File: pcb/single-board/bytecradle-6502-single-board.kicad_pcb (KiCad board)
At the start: 2 copper layers, 224.9 x 116.2 mm, 88 parts, among them J1 USB_B, J2 EXPBUS1, J3 EXPBUS2, J4 VIA, J5 UART1, J6 UART2, J7 Serial, J8 Serial, SW1 SW_SPDT, SW2 RESET, SW3 NMI, U1 74HC14, U10 74HC273, U11 74HC273, U12 74HC245, U13 74HC245, U14 74HC10, U15 SST39SF040, U16 AS6C4008, U17 CY62256, U18 74HC688, U19 W65C22NxP, U2 W65C02, U20 74HC688, U21 W65C51NxP, U22 74HC688, U23 W65C51NxP, U3 74HC688, U4 74HC08, U5 74HC688, U6 74HC688, U7 74HC04, U8 74HC10, U9 74HC00, X1 32MHz, Y1 1.8432 MHz, Y2 1.8432 MHz

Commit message: Further revising
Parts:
- added G***: LOGO, components:bytecradle-logo, F.Cu at (256.4, 48.5)
- X1: value 32MHz -> 14 MHz
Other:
- board text added: "jlcjlcjlcjlc"

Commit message: Updating design for V2
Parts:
- U1: value 74HC14 -> 74AC14
- U14, U8: value 74HC10 -> 74AC10
- U16: value AS6C4008 -> AS6C4008-55
- U17: value CY62256 -> 62256-55
- U18, U20, U22, U3, U5, U6: value 74HC688 -> CD74HC688
- U4: value 74HC08 -> 74AC08
- U7: value 74HC04 -> 74AC04
- U9: value 74HC00 -> 74AC00
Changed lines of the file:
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@@
 			)
 		)
-		(property "Value" "74HC688"
+		(property "Value" "CD74HC688"
 			(at 3.81 25.19 -90)
 			(layer "F.SilkS")
@@
 			)
 		)
-		(property "Value" "74HC688"
+		(property "Value" "CD74HC688"
 			(at 3.81 25.19 0)
 			(layer "F.SilkS")
@@
 		(property "Value" "100nF"
 			(at 2.5 2.54 90)
-			(layer "F.SilkS")
+			(layer "Dwgs.User")
 			(effects
 				(font
@@
 			)
 		)
-		(property "Value" "CY62256"
+		(property "Value" "62256-55"
 			(at 7.62 35.35 -90)
 			(layer "F.SilkS")
@@
 			)
 		)
-		(property "Value" "74HC688"
+		(property "Value" "CD74HC688"
 			(at 3.81 25.19 90)
-			(layer "F.Fab")
+			(layer "F.SilkS")
 			(effects
 				(font
@@
 			)
 		)
-		(property "Value" "74HC688"
+		(property "Value" "CD74HC688"
 			(at 3.81 25.19 -90)
 			(layer "F.SilkS")
@@
 			)
 		)
-		(property "Value" "74HC04"
+		(property "Value" "74AC04"
 			(at 3.81 17.57 -90)
 			(layer "F.SilkS")
@@
 			)
 		)
-		(property "Value" "AS6C4008"
+		(property "Value" "AS6C4008-55"
 			(at 7.62 40.43 90)
 			(layer "F.SilkS")
@@
 			)
 		)
-		(property "Value" "74HC10"
+		(property "Value" "74AC10"
 			(at 3.81 17.57 90)
 			(layer "F.SilkS")
@@
 			)
 		)
-		(property "Value" "74HC08"
+		(property "Value" "74AC08"
 			(at 3.81 17.57 -90)
 			(layer "F.SilkS")
@@
 			)
 		)
-		(property "Value" "74HC688"
+		(property "Value" "CD74HC688"
 			(at 3.81 25.19 0)
 			(layer "F.SilkS")
@@
 			)
 		)
-		(property "Value" "74HC10"
+		(property "Value" "74AC10"
 			(at 3.81 17.57 -90)
 			(layer "F.SilkS")
@@
 			)
 		)
-		(property "Value" "74HC14"
+		(property "Value" "74AC14"
 			(at 3.81 17.57 -90)
 			(layer "F.SilkS")
@@
 			)
 		)
-		(property "Value" "74HC00"
+		(property "Value" "74AC00"
 			(at 3.81 17.57 -90)
 			(layer "F.SilkS")
@@
 			)
 		)
-		(property "Value" "74HC688"
+		(property "Value" "CD74HC688"
 			(at 3.81 25.19 90)
 			(layer "F.SilkS")

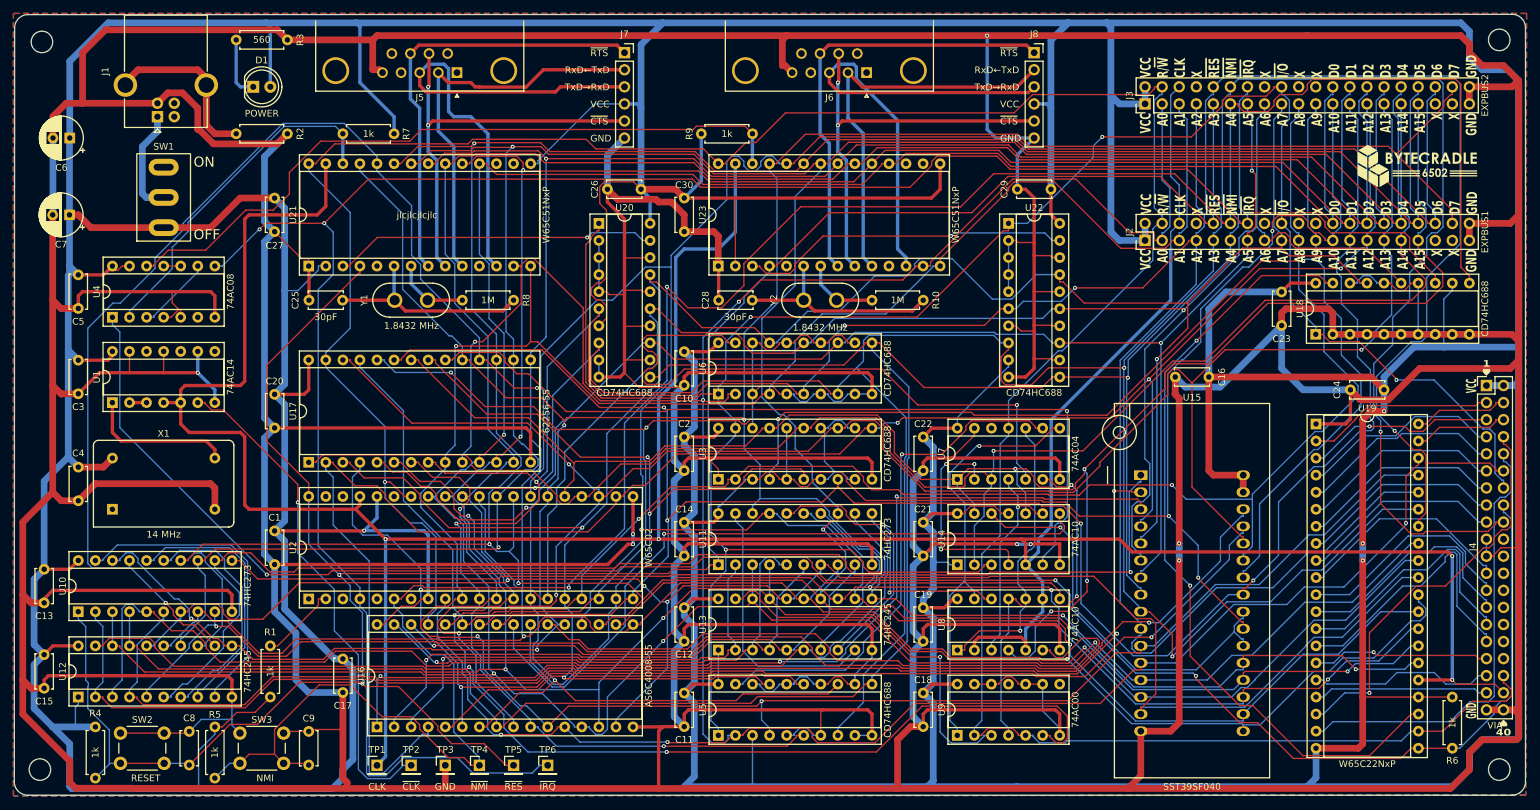
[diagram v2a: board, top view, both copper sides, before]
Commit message: Revising single board layout
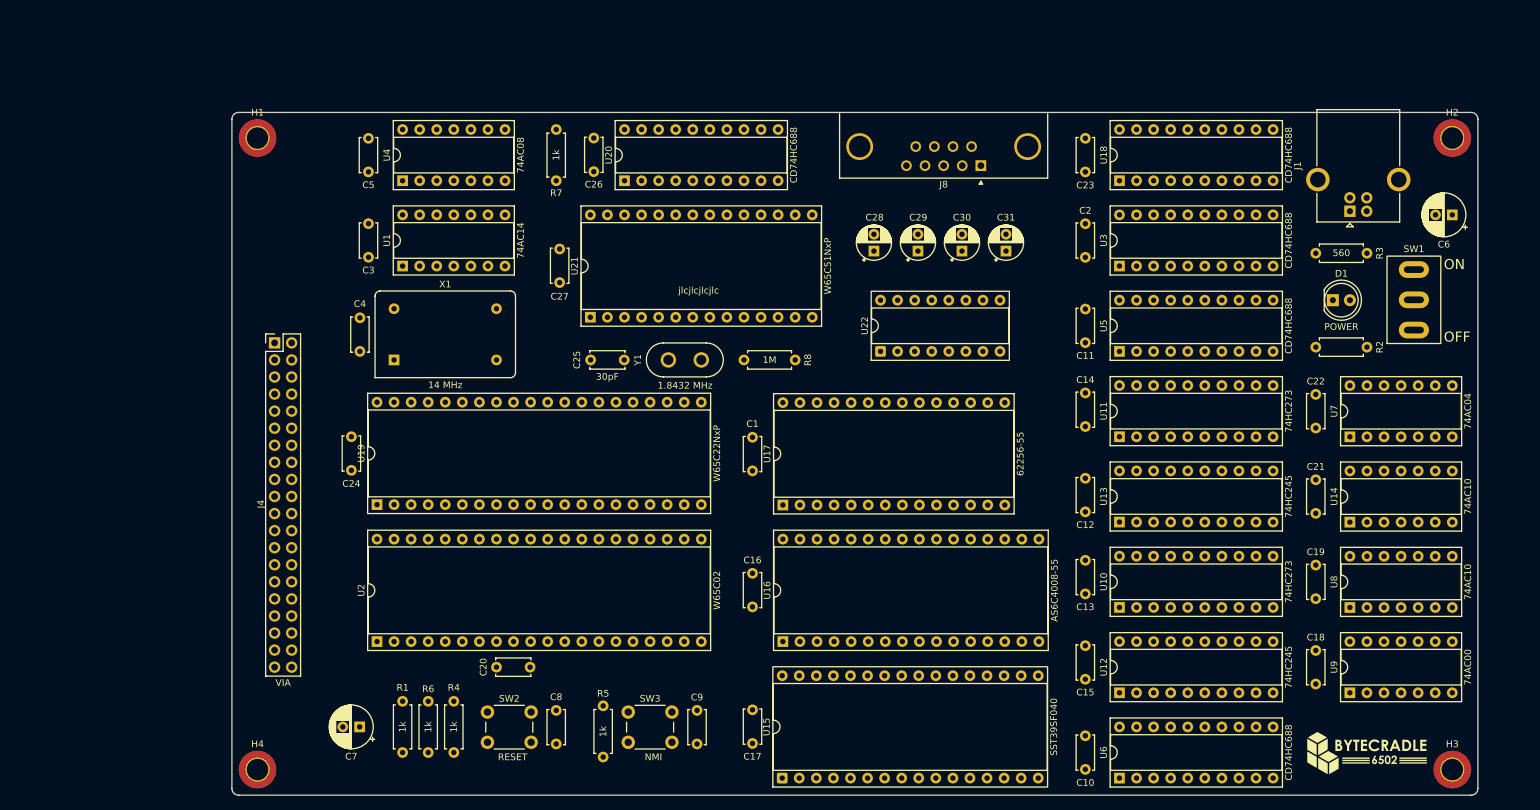
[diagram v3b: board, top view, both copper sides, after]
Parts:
- removed J2: EXPBUS1, Connector_PinHeader_2.54mm:PinHeader_2x20_P2.54mm_Vertical
- removed J3: EXPBUS2, Connector_PinHeader_2.54mm:PinHeader_2x20_P2.54mm_Vertical
- removed J5: UART1, Connector_Dsub:DSUB-9_Male_Horizontal_P2.77x2.84mm_EdgePinOffset4.94mm_Housed_MountingHolesOffset7.48mm
- removed J6: UART2, Connector_Dsub:DSUB-9_Male_Horizontal_P2.77x2.84mm_EdgePinOffset4.94mm_Housed_MountingHolesOffset7.48mm
- removed J7: Serial, Connector_PinSocket_2.54mm:PinSocket_1x06_P2.54mm_Vertical
- removed R10: 1M, Resistor_THT:R_Axial_DIN0207_L6.3mm_D2.5mm_P7.62mm_Horizontal
- removed R9: 1k, Resistor_THT:R_Axial_DIN0207_L6.3mm_D2.5mm_P7.62mm_Horizontal
- removed TP1: CLK, Connector_PinHeader_2.54mm:PinHeader_1x01_P2.54mm_Vertical
- removed TP2: ~{CLK}, Connector_PinHeader_2.54mm:PinHeader_1x01_P2.54mm_Vertical
- removed TP3: GND, Connector_PinHeader_2.54mm:PinHeader_1x01_P2.54mm_Vertical
- removed TP4: ~{NMI}, Connector_PinHeader_2.54mm:PinHeader_1x01_P2.54mm_Vertical
- removed TP5: ~{RES}, Connector_PinHeader_2.54mm:PinHeader_1x01_P2.54mm_Vertical
- removed TP6: ~{IRQ}, Connector_PinHeader_2.54mm:PinHeader_1x01_P2.54mm_Vertical
- removed U23: W65C51NxP, Package_DIP:DIP-28_W15.24mm_Socket
- removed Y2: 1.8432 MHz, Crystal:Crystal_HC50_Vertical
- added C31: 10uF, Capacitor_THT:CP_Radial_D5.0mm_P2.50mm, F.Cu at (195.2, 61.3)
- C28: value 30pF -> 10uF; footprint Capacitor_THT:C_Disc_D5.0mm_W2.5mm_P5.00mm -> Capacitor_THT:CP_Radial_D5.0mm_P2.50mm
- C29, C30: value 100nF -> 10uF; footprint Capacitor_THT:C_Disc_D5.0mm_W2.5mm_P5.00mm -> Capacitor_THT:CP_Radial_D5.0mm_P2.50mm
- C6: value 10uF -> 100uF
- H1, H2, H3, H4: footprint MountingHole:MountingHole_3.2mm_M3 -> MountingHole:MountingHole_3.2mm_M3_DIN965_Pad_TopOnly
- J8: value Serial -> UART1; footprint Connector_PinSocket_2.54mm:PinSocket_1x06_P2.54mm_Vertical -> Connector_Dsub:DSUB-9_Pins_Horizontal_P2.77x2.84mm_EdgePinOffset4.94mm_Housed_MountingHolesOffset4.94mm
- U15: footprint Socket:DIP_Socket-32_W11.9_W12.7_W15.24_W17.78_W18.5_3M_232-1285-00-0602J -> Package_DIP:DIP-32_W15.24mm_Socket
- U22: value CD74HC688 -> MAX232; footprint Package_DIP:DIP-20_W7.62mm_Socket -> Package_DIP:DIP-16_W7.62mm_Socket
- moved H3 210.2 mm to (261.6, 138.4)
- moved C6 206.1 mm to (261.6, 55.9)
- moved SW1 186.7 mm to (255.9, 68.5)
- moved H4 184.8 mm to (83.8, 138.4)
- moved J4 180.5 mm to (86.4, 74.9)
- moved J1 178.0 mm to (246.4, 55.3)
- moved D1 163.8 mm to (243.8, 68.6)
- moved R2 163.8 mm to (248.9, 75.6)
- moved R3 163.8 mm to (248.9, 61.6)
- moved C13 154.9 mm to (207.0, 107.3)
- moved C15 154.9 mm to (207.0, 120.0)
- moved U10 154.9 mm to (212.1, 114.3)
- moved U12 154.9 mm to (212.1, 127.0)
- moved C24 153.8 mm to (97.8, 88.9), turned to -90 degrees
- moved R6 152.6 mm to (109.2, 135.9), turned to 90 degrees
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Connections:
- C28 pad 1: GND -> Net-(U22-C1+)
- C28 pad 2: Net-(U23-XTAL1) -> Net-(U22-C1-)
- C29 pad 1: VCC -> Net-(U22-C2+)
- C29 pad 2: GND -> Net-(U22-C2-)
- C30 pad 1: VCC -> Net-(U22-VS+)
- C30 pad 2: GND -> VCC
- J8 pad 1: ~{RTS2} -> unconnected-(J8-Pad1)
- J8 pad 2: TxD2 -> Net-(U22-T1OUT)
- J8 pad 3: RxD2 -> Net-(U22-R1IN)
- J8 pad 4: VCC -> unconnected-(J8-Pad4)
- J8 pad 5: ~{CTS2} -> GND
- J8 pad 6: GND -> unconnected-(J8-Pad6)
- U21 pad 8: ~{RTS1} -> GND
- U21 pad 9: ~{CTS1} -> GND
- U22 pad 1: ~{I/O} -> Net-(U22-C1+)
- U22 pad 10: GND -> unconnected-(U22-T2IN-Pad10)
- U22 pad 11: A4 -> TxD1
- U22 pad 12: GND -> RxD1
- U22 pad 13: A5 -> Net-(U22-R1IN)
- U22 pad 14: GND -> Net-(U22-T1OUT)
- U22 pad 15: A6 -> GND
- U22 pad 16: GND -> VCC
- U22 pad 2: GND -> Net-(U22-VS+)
- U22 pad 3: GND -> Net-(U22-C1-)
- U22 pad 4: GND -> Net-(U22-C2+)
- U22 pad 5: GND -> Net-(U22-C2-)
- U22 pad 6: A2 -> Net-(U22-VS-)
- U22 pad 7: GND -> unconnected-(U22-T2OUT-Pad7)
- U22 pad 8: A3 -> unconnected-(U22-R2IN-Pad8)
- U22 pad 9: VCC -> unconnected-(U22-R2OUT-Pad9)
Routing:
- net GND: track 2097.2 -> 0.00 mm, vias 8 -> 0
- net VCC: track 1595.0 -> 0.00 mm, vias 4 -> 0
- net D6: track 565.5 -> 0.00 mm, vias 5 -> 0
- net D4: track 523.2 -> 0.00 mm, vias 4 -> 0
- net D5: track 513.6 -> 0.00 mm, vias 6 -> 0
- net CLK: track 507.3 -> 0.00 mm, vias 4 -> 0
- net ~{RES}: track 500.8 -> 0.00 mm, vias 3 -> 0
- net D2: track 495.5 -> 0.00 mm, vias 3 -> 0
- net D7: track 493.3 -> 0.00 mm, vias 6 -> 0
- net D3: track 492.8 -> 0.00 mm, vias 3 -> 0
- net D0: track 482.4 -> 0.00 mm, vias 4 -> 0
- net D1: track 482.1 -> 0.00 mm, vias 5 -> 0
- net A0: track 441.5 -> 0.00 mm, vias 6 -> 0
- net R/~{W}: track 419.2 -> 0.00 mm, vias 1 -> 0
- net ~{NMI}: track 408.5 -> 0.00 mm, vias 3 -> 0
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- removed copper zone on F.Cu, net GND
- removed copper zone on B.Cu, net VCC
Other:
- board size 224.9 x 116.2 mm -> 185.4 x 101.6 mm
- board text removed: "1"
- board text removed: "40"
- board text removed: "GND"
- board text removed: "RxD←TxD"
- board text removed: "TxD→RxD"
- board text removed: "VCC"
- board text removed: "VCC A0 A1 A2 A3 A4 A5 A6 A7 A8 A9 A10 A11 A12 A13 A14 A15 X X GND"
- board text removed: "VCC R/~{W} CLK X ~{RES} ~{NMI} ~{IRQ} X ~{I/O} X X D0 D1 D2 D3 D4 D5 D6 D7 GND"
- board text removed: "~{CTS}"
- board text removed: "~{RTS}"

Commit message: Routing
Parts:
- added C32: 100nF, Capacitor_THT:C_Disc_D5.0mm_W2.5mm_P5.00mm, F.Cu at (171.4, 59.7)
- moved C30 16.5 mm to (181.6, 76.2)
- moved C29 16.0 mm to (188.0, 76.2)
- moved C31 14.9 mm to (194.3, 76.2)
- moved C28 14.9 mm to (175.3, 76.2)
- moved U22 10.2 mm to (176.5, 66.0)
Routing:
- net GND: track 0.00 -> 247.9 mm
- net CLK: track 0.00 -> 128.1 mm
- net VCC: track 0.00 -> 43.3 mm
- net Net-(X1-OUT): track 0.00 -> 16.6 mm
- net Net-(U22-C2+): track 0.00 -> 13.2 mm
- net Net-(U22-T1OUT): track 0.00 -> 12.8 mm
- net Net-(U22-VS+): track 0.00 -> 12.0 mm
- net Net-(U22-C1-): track 0.00 -> 11.7 mm
- net Net-(U22-C1+): track 0.00 -> 10.6 mm
- net Net-(U22-R1IN): track 0.00 -> 10.6 mm
- net Net-(U22-VS-): track 0.00 -> 10.5 mm
- net Net-(U22-C2-): track 0.00 -> 8.15 mm
- net Net-(U1-Pad2): track 0.00 -> 2.54 mm

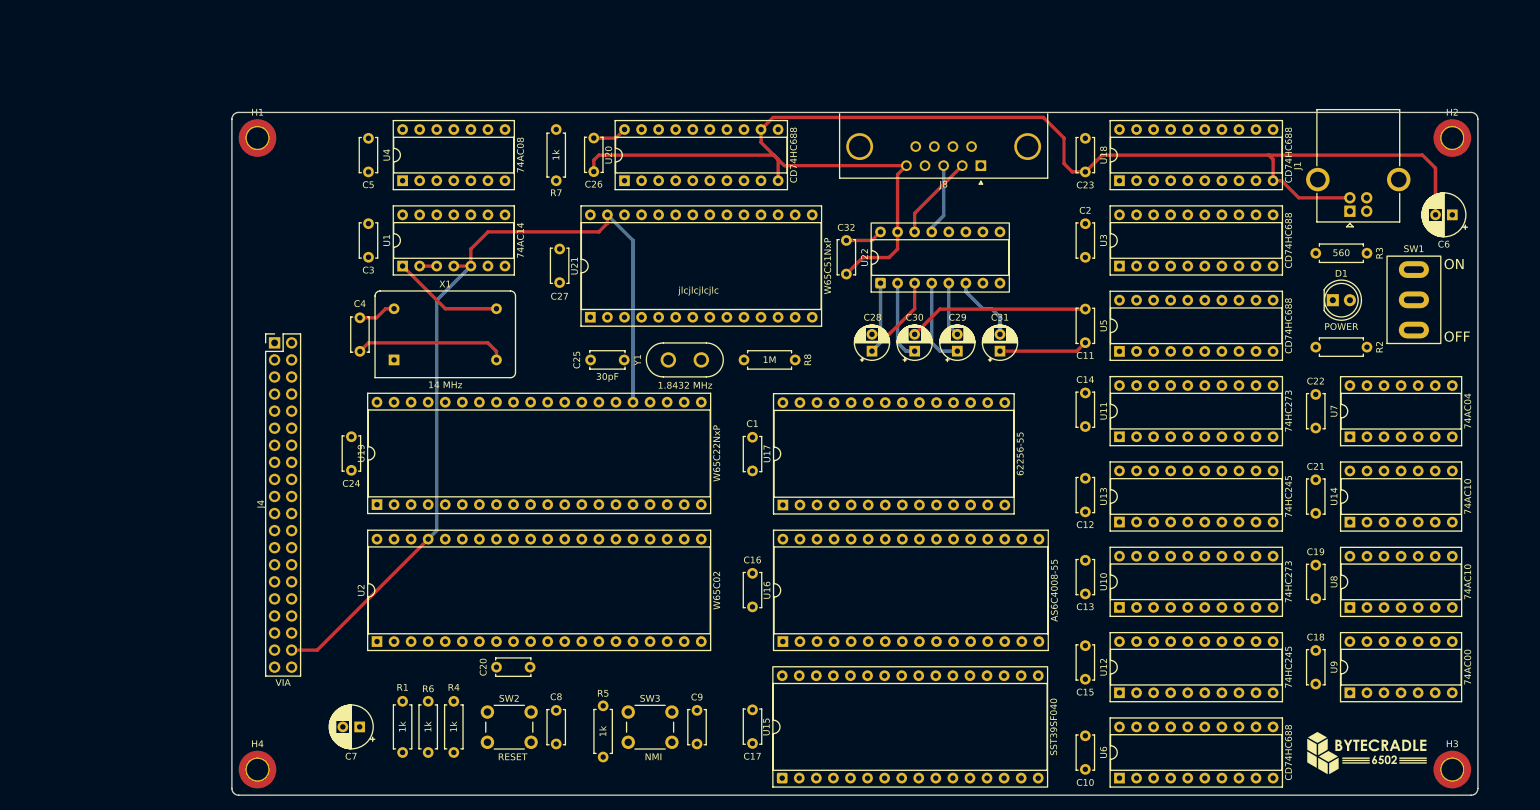
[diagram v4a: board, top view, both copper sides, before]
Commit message: Initial commit bitbang SD-card routines
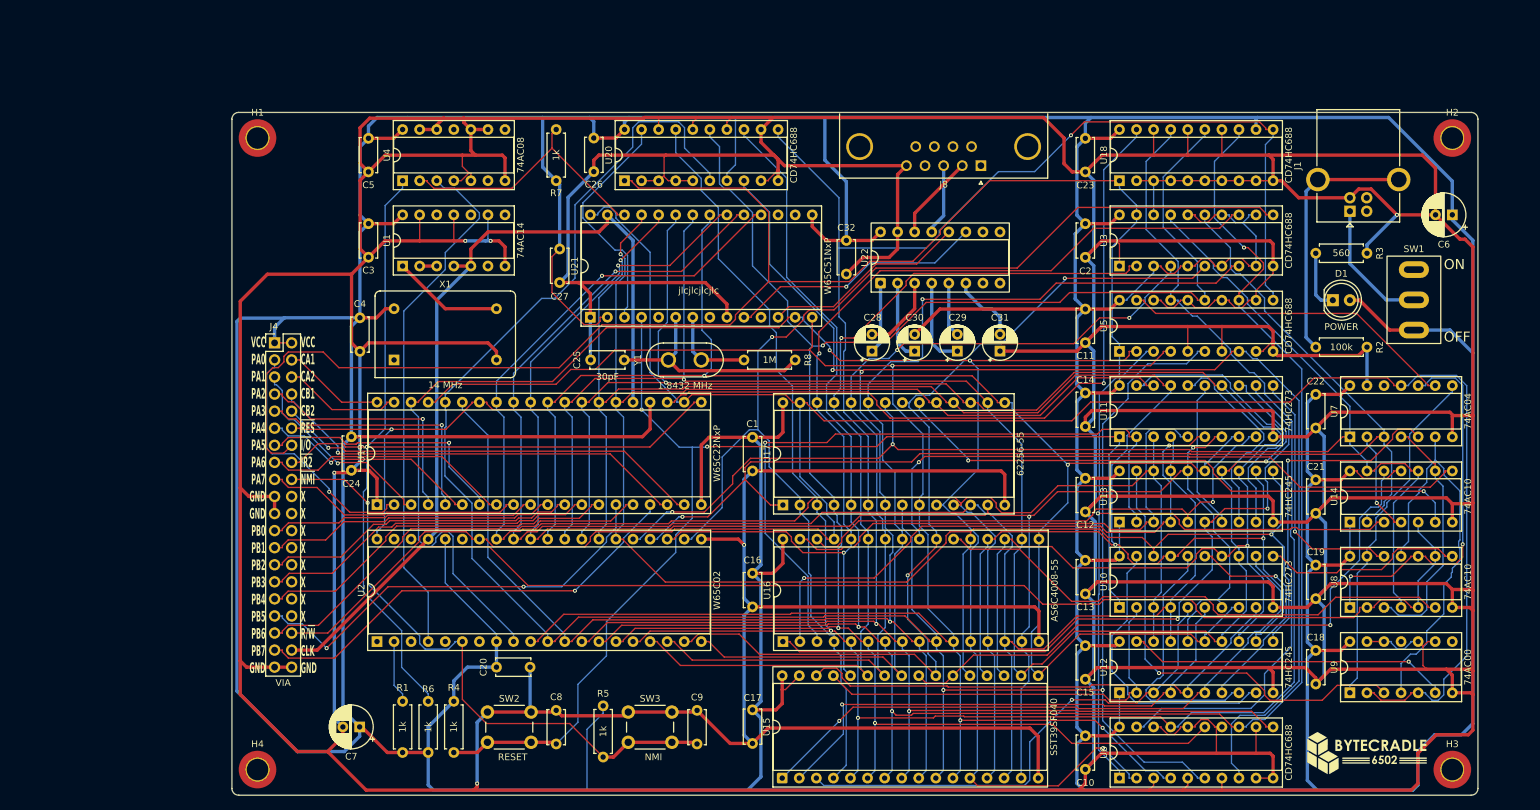
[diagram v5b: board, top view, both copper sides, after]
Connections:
- U21 pad 8: GND -> unconnected-(U21-~{RTS}-Pad8)
- U4 pad 10: Net-(U4-Pad10) -> GND
- U4 pad 11: Net-(U4-Pad10) -> unconnected-(U4-Pad11)
- U4 pad 12: ~{IRQC51_2} -> GND
- U4 pad 13: VCC -> GND
- U4 pad 3: Net-(U4-Pad3) -> ~{IRQ}
- U4 pad 8: ~{IRQ} -> unconnected-(U4-Pad8)
- U4 pad 9: Net-(U4-Pad3) -> GND
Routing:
- net GND: track 247.9 -> 1877.3 mm, vias 0 -> 6
- net VCC: track 43.3 -> 1308.3 mm
- net R/~{W}: track 0.00 -> 335.1 mm
- net ~{I/O}: track 0.00 -> 330.8 mm, vias 0 -> 1
- net A3: track 0.00 -> 329.3 mm, vias 0 -> 3
- net A2: track 0.00 -> 326.2 mm, vias 0 -> 2
- net A5: track 0.00 -> 306.5 mm, vias 0 -> 3
- net A4: track 0.00 -> 306.5 mm, vias 0 -> 3
- net A7: track 0.00 -> 303.3 mm, vias 0 -> 2
- net D7: track 0.00 -> 295.2 mm, vias 0 -> 2
- net A1: track 0.00 -> 288.9 mm, vias 0 -> 3
- net A6: track 0.00 -> 288.3 mm, vias 0 -> 3
- net D6: track 0.00 -> 267.8 mm, vias 0 -> 3
- net A0: track 0.00 -> 264.4 mm, vias 0 -> 3
- net D5: track 0.00 -> 260.7 mm, vias 0 -> 2
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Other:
- board text added: "VCC CA1 CA2 CB1 CB2 ~{RES} ~{I/O} ~{IR2} ~{NMI} X X X X X X X X R/~{W} CLK GND"
- board text added: "VCC PA0 PA1 PA2 PA3 PA4 PA5 PA6 PA7 GND GND PB0 PB1 PB2 PB3 PB4 PB5 PB6 PB7 GND"
